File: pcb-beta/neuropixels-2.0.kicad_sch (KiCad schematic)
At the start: 12 parts, among them J2 046844727002846+, J3 046844727002846+, U4 TS5A3159AYZPR, U5 ECS-2016MV-480-CN-TR

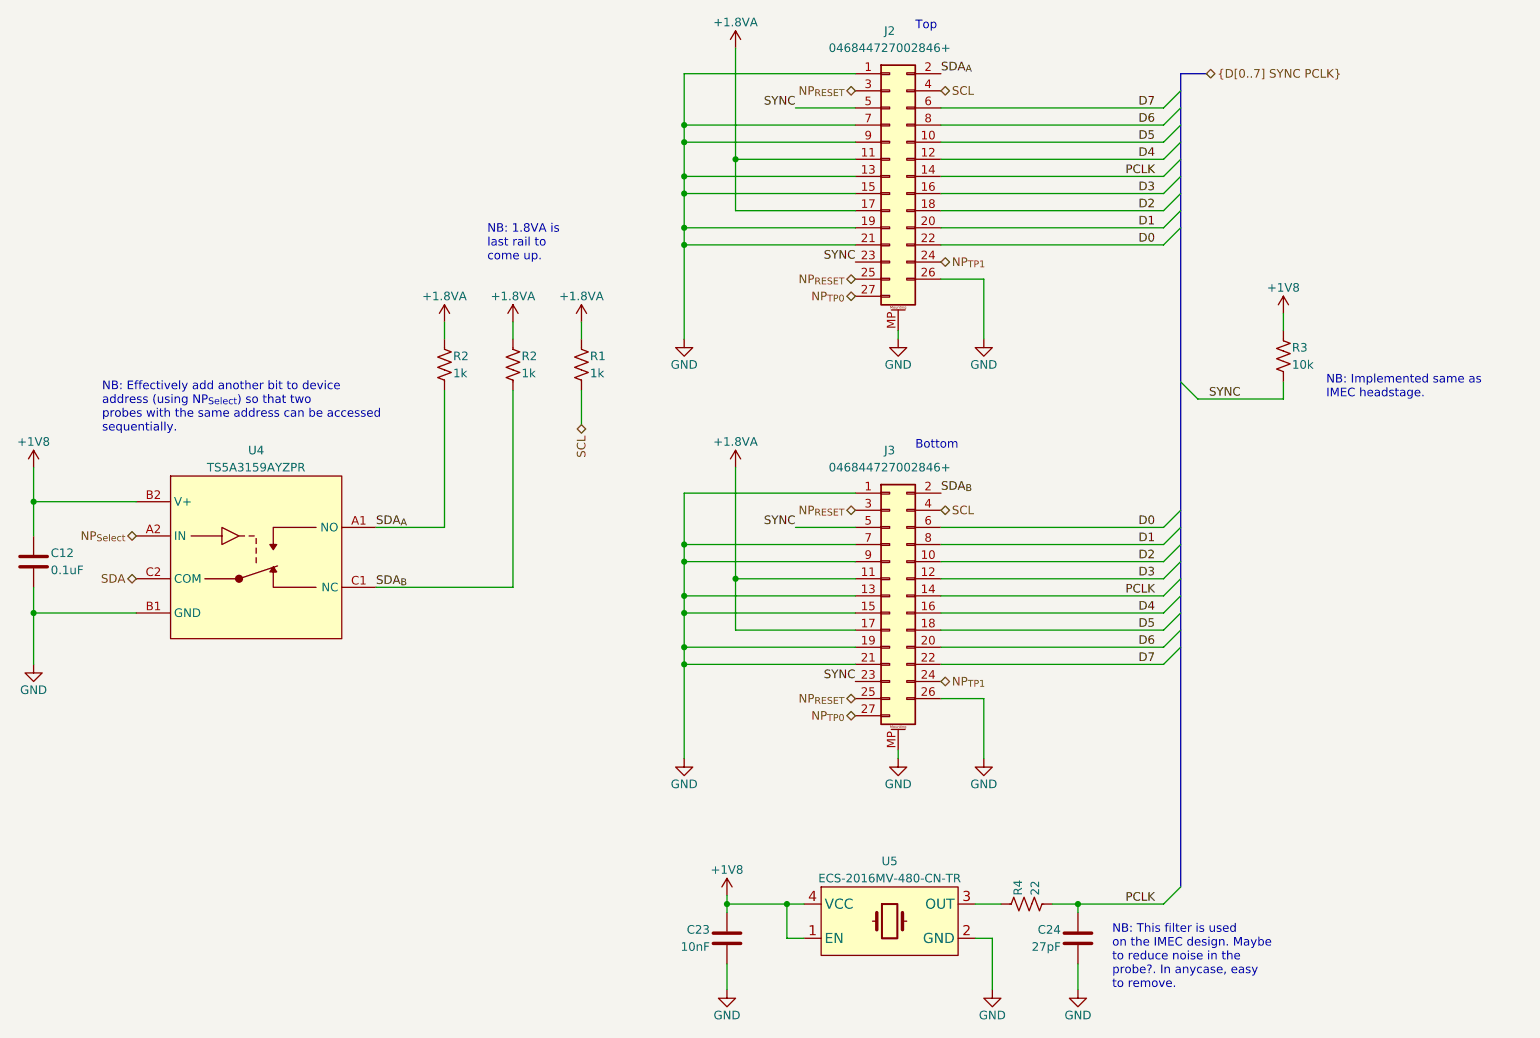
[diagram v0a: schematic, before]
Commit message: Move pcb to pcb-beta directory
- Because this board only works with Beta-test NP2.0 probes
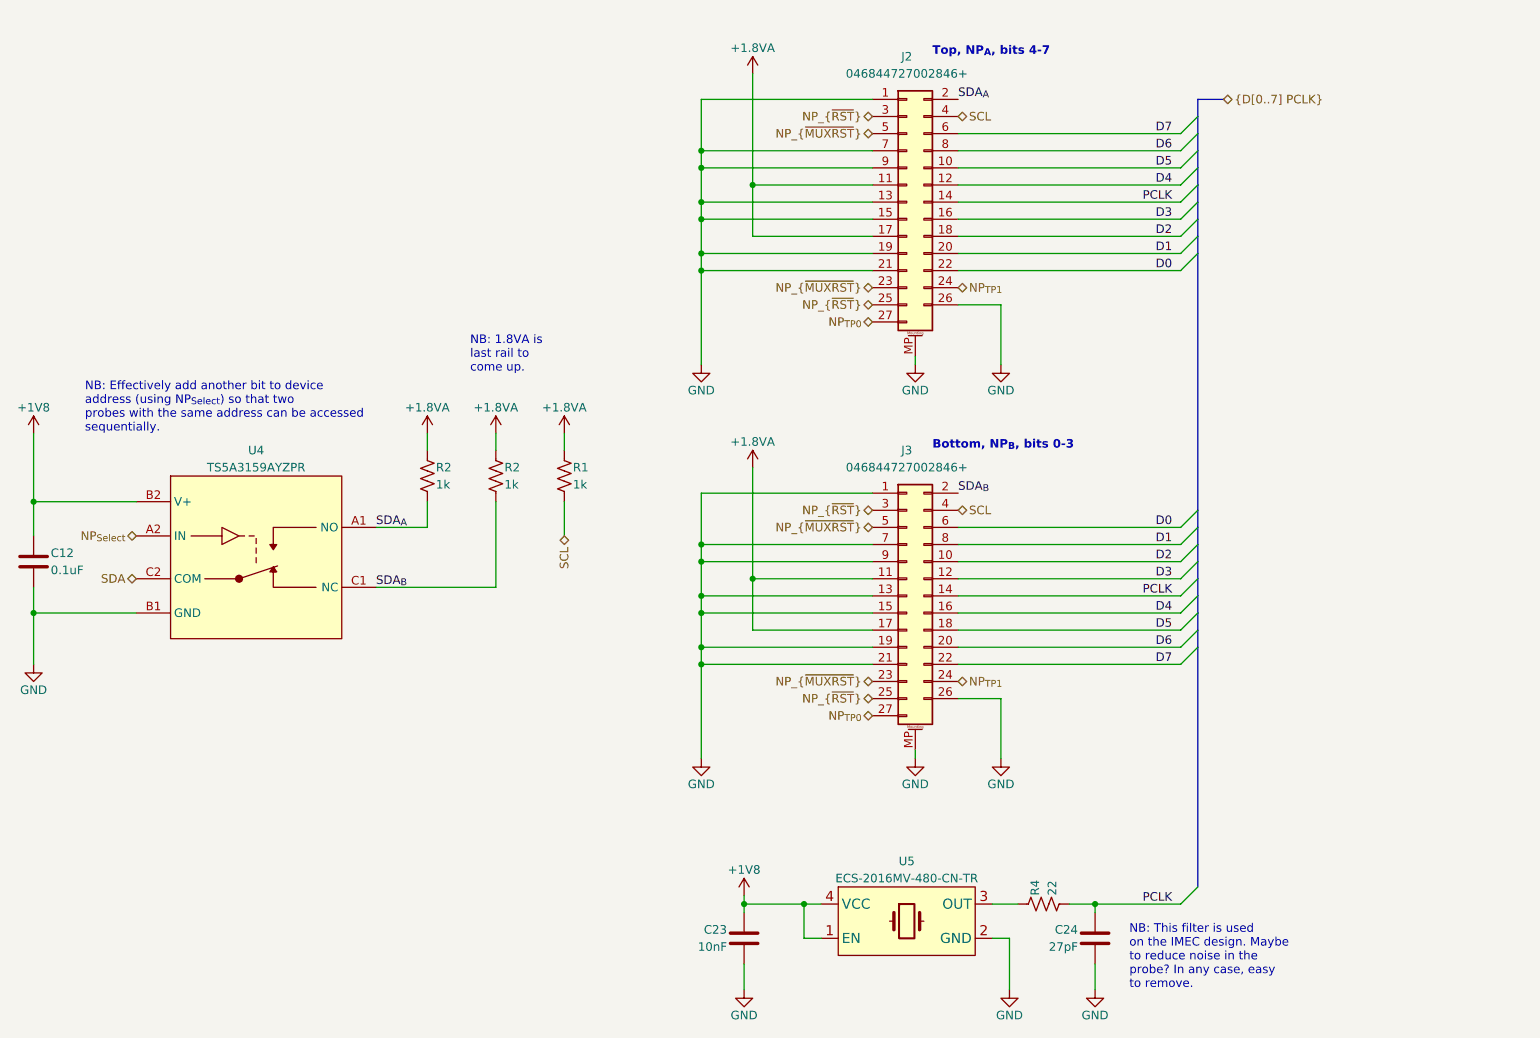
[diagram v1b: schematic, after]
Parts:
- removed R3: 10k, Resistor_SMD:R_0201_0603Metric, symbol Device:R_US
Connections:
- net NP_{RESET} renamed NP_{~{RST}}
- net SYNC renamed NP_{~{MUXRST}}
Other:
- note added: "Bottom, NP_{B}, bits 0-3"
- note added: "NB: This filter is used on the IMEC design. Maybe to reduce noise in the probe? In any case, easy to remove."
- note added: "Top, NP_{A}, bits 4-7"
- note removed: "Bottom"
- note removed: "NB: Implemented same as IMEC headstage."
- note removed: "NB: This filter is used on the IMEC design. Maybe to reduce noise in the probe?. In anycase, easy to remove."
- note removed: "Top"
- moved on the sheet: C23, C24, J2, J3, R1, R2, R4, U5
